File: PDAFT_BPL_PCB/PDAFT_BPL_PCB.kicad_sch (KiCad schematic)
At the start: 16 parts

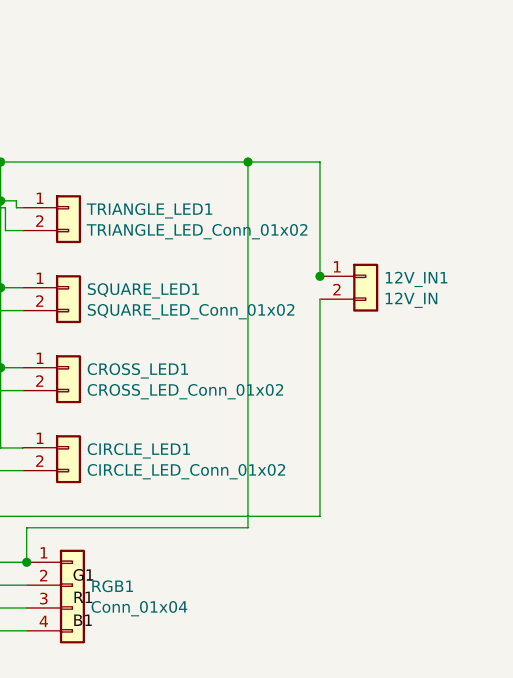
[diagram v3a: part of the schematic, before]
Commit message: Changing 12vin JST XH2 to XH4
Changing 12Vin JST XH2 to XH4 because of possible current rating limits 3A, so better to parallelize 12Vin to avoid problems with it
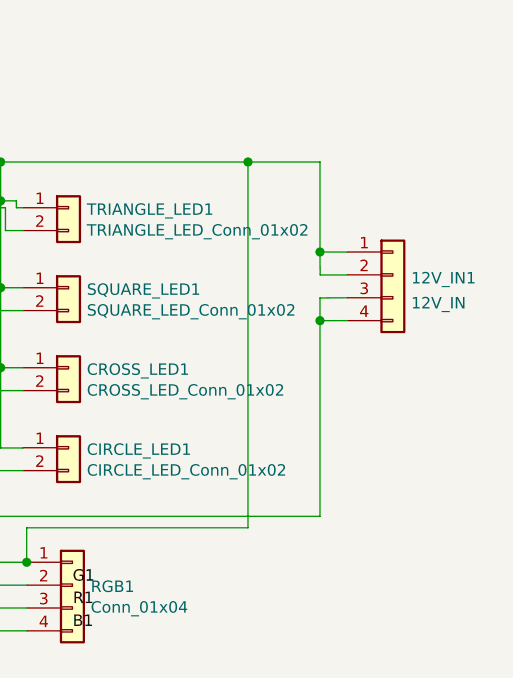
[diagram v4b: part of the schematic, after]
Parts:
- removed 12V_IN1: 12V_IN, Connector_JST:JST_XH_B2B-XH-A_1x02_P2.50mm_Vertical, symbol Connector_Generic:Conn_01x02
- added 12V_IN1: 12V_IN, Connector_JST:JST_XH_B4B-XH-A_1x04_P2.50mm_Vertical, symbol Connector_Generic:Conn_01x04
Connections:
- net at Circle1.3 (Pin_3), Cross1.3 (Pin_3), ProMicro1.23 (GND)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: now also 12V_IN1.3 (Pin_3), 12V_IN1.4 (Pin_4)
- net at CIRCLE_LED1.1 (Pin_1), CROSS_LED1.1 (Pin_1), RGB1.1 (Pin_1)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: now also 12V_IN1.1 (Pin_1), 12V_IN1.2 (Pin_2)
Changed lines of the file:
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@@
   (junction (at 217.6018 85.1154) (diameter 1.016) (color 0 0 0 0))
   (junction (at 242.189 40.64) (diameter 1.016) (color 0 0 0 0))
-  (junction (at 250.19 53.34) (diameter 1.016) (color 0 0 0 0))
+  (junction (at 250.19 50.6406) (diameter 1.016) (color 0 0 0 0))
+  (junction (at 250.19 58.2723) (diameter 1.016) (color 0 0 0 0))
   (wire (pts (xy 43.0276 40.7162) (xy 43.0276 63.3222))
     (stroke (width 0) (type solid) (color 0 0 0 0))
@@
     (stroke (width 0) (type solid) (color 0 0 0 0))
   )
-  (wire (pts (xy 250.19 40.64) (xy 250.19 53.34))
-    (stroke (width 0) (type solid) (color 0 0 0 0))
-  )
-  (wire (pts (xy 250.19 53.34) (xy 250.19 53.3654))
-    (stroke (width 0) (type solid) (color 0 0 0 0))
-  )
-  (wire (pts (xy 250.19 55.88) (xy 250.19 80.01))
+  (wire (pts (xy 250.19 40.64) (xy 250.19 50.6406))
+    (stroke (width 0) (type solid) (color 0 0 0 0))
+  )
+  (wire (pts (xy 250.19 50.6406) (xy 250.19 50.6463))
+    (stroke (width 0) (type solid) (color 0 0 0 0))
+  )
+  (wire (pts (xy 250.19 50.6406) (xy 250.2094 53.1851))
+    (stroke (width 0) (type solid) (color 0 0 0 0))
+  )
+  (wire (pts (xy 250.19 55.7447) (xy 250.19 58.2723))
+    (stroke (width 0) (type solid) (color 0 0 0 0))
+  )
+  (wire (pts (xy 250.19 55.7447) (xy 253.2055 55.7251))
+    (stroke (width 0) (type solid) (color 0 0 0 0))
+  )
+  (wire (pts (xy 250.19 58.2723) (xy 250.19 80.01))
+    (stroke (width 0) (type solid) (color 0 0 0 0))
+  )
+  (wire (pts (xy 250.2094 53.1851) (xy 253.2055 53.1851))
+    (stroke (width 0) (type solid) (color 0 0 0 0))
+  )
+  (wire (pts (xy 253.2055 50.6451) (xy 250.19 50.6463))
+    (stroke (width 0) (type solid) (color 0 0 0 0))
+  )
+  (wire (pts (xy 253.2055 58.2651) (xy 250.19 58.2723))
     (stroke (width 0) (type solid) (color 0 0 0 0))
   )
@@
     )
     (property "Datasheet" "~" (id 3) (at 222.25 72.39 0)
-      (effects (font (size 1.27 1.27)) hide)
-    )
-    (pin "1")
-    (pin "2")
-  )
-  (symbol (lib_id "Connector_Generic:Conn_01x02") (at 255.27 53.34 0) (unit 1)
-    (in_bom yes) (on_board yes)
-    (property "Reference" "12V_IN1" (id 0) (at 257.302 53.5432 0)
-      (effects (font (size 1.27 1.27)) (justify left))
-    )
-    (property "Value" "12V_IN" (id 1) (at 257.302 55.8546 0)
-      (effects (font (size 1.27 1.27)) (justify left))
-    )
-    (property "Footprint" "Connector_JST:JST_XH_B2B-XH-A_1x02_P2.50mm_Vertical" (id 2) (at 255.27 53.34 0)
-      (effects (font (size 1.27 1.27)) hide)
-    )
-    (property "Datasheet" "~" (id 3) (at 255.27 53.34 0)
       (effects (font (size 1.27 1.27)) hide)
     )
@@
     )
     (property "Datasheet" "~" (id 3) (at 222.6818 87.6554 0)
+      (effects (font (size 1.27 1.27)) hide)
+    )
+    (pin "1")
+    (pin "2")
+    (pin "3")
+    (pin "4")
+  )
+  (symbol (lib_id "Connector_Generic:Conn_01x04") (at 258.2855 53.1851 0) (unit 1)
+    (in_bom yes) (on_board yes) (fields_autoplaced)
+    (property "Reference" "12V_IN1" (id 0) (at 260.3176 53.5466 0)
+      (effects (font (size 1.27 1.27)) (justify left))
+    )
+    (property "Value" "12V_IN" (id 1) (at 260.3176 56.3217 0)
+      (effects (font (size 1.27 1.27)) (justify left))
+    )
+    (property "Footprint" "Connector_JST:JST_XH_B4B-XH-A_1x04_P2.50mm_Vertical" (id 2) (at 258.2855 53.1851 0)
+      (effects (font (size 1.27 1.27)) hide)
+    )
+    (property "Datasheet" "~" (id 3) (at 258.2855 53.1851 0)
       (effects (font (size 1.27 1.27)) hide)
     )
@@
   )
   (symbol_instances
-    (path "/00000000-0000-0000-0000-00005dc75aa5"
-      (reference "12V_IN1") (unit 1) (value "12V_IN") (footprint "Connector_JST:JST_XH_B2B-XH-A_1x02_P2.50mm_Vertical")
+    (path "/bfd26073-15dd-489a-abdd-d9c873eed720"
+      (reference "12V_IN1") (unit 1) (value "12V_IN") (footprint "Connector_JST:JST_XH_B4B-XH-A_1x04_P2.50mm_Vertical")
     )
     (path "/00000000-0000-0000-0000-00005dc6eebc"

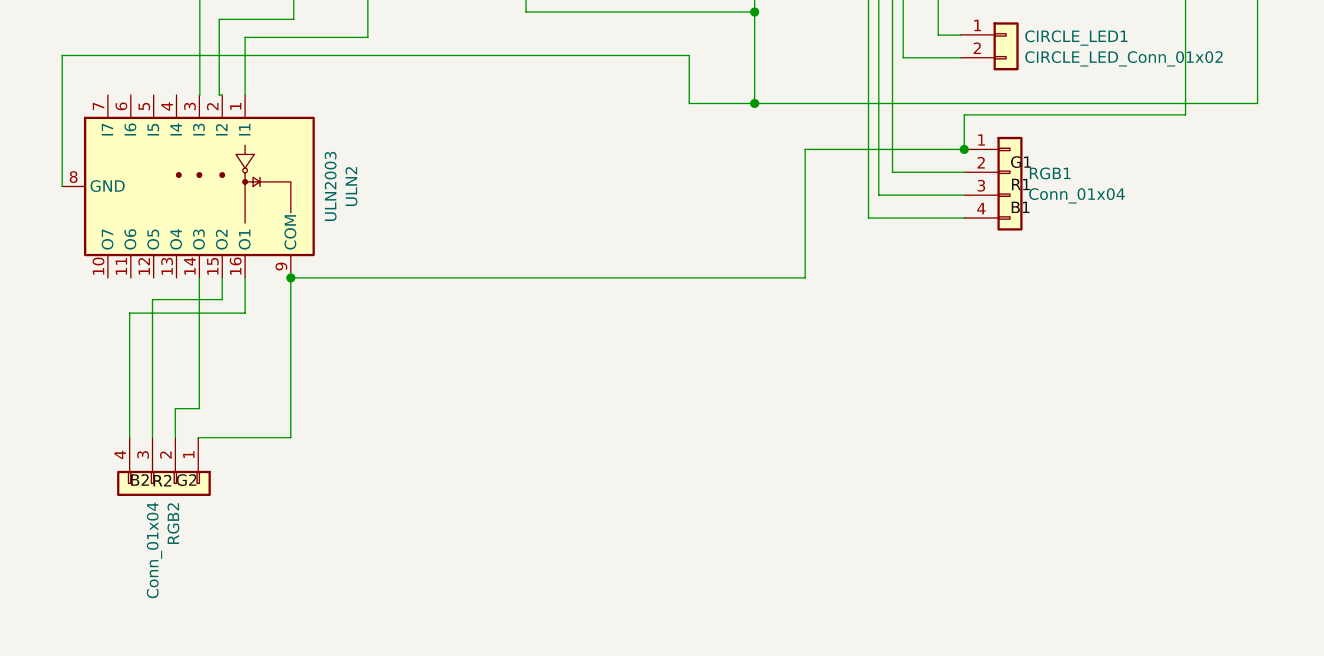
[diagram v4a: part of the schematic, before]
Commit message: Firmware update
Firmware updated (USB-Serial and serial1 different firmware files), added 3D-model of Arduino for picture, pictures added, readme updated
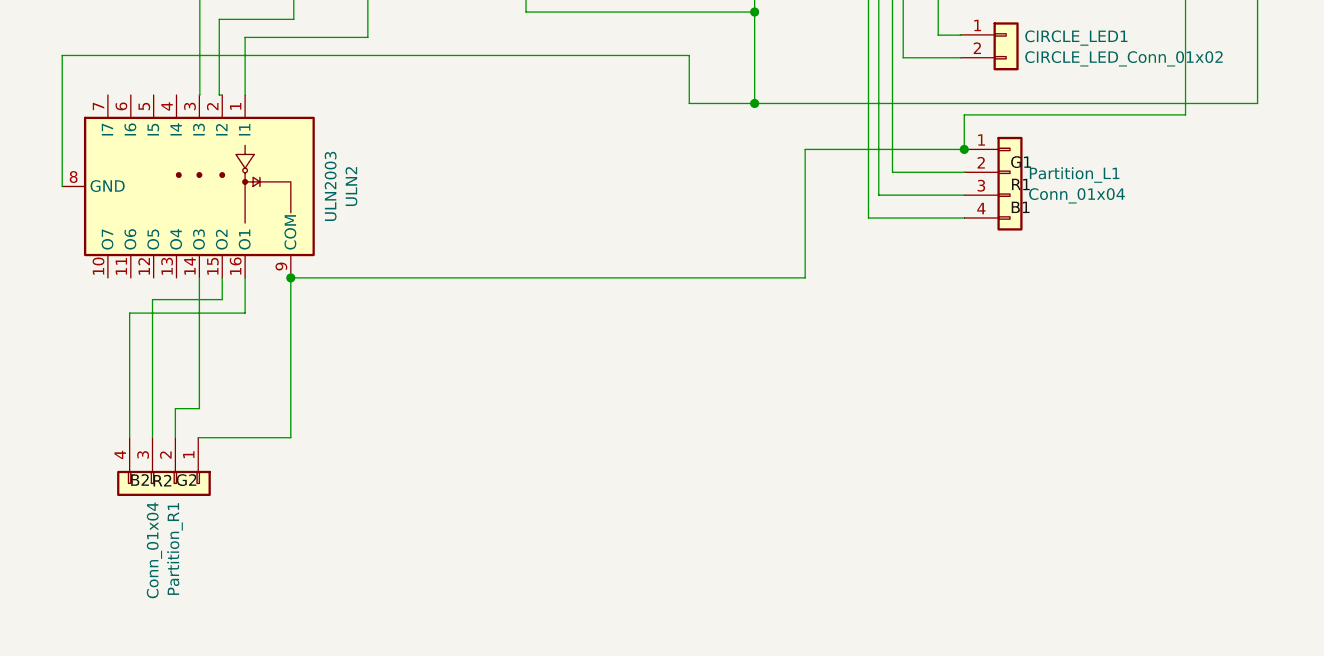
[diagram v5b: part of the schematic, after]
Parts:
- renumbered RGB1 to Partition_L1, RGB2 to Partition_R1
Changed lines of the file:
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@@
   (symbol (lib_id "Connector_Generic:Conn_01x04") (at 129.9464 122.2248 270) (unit 1)
     (in_bom yes) (on_board yes)
-    (property "Reference" "RGB2" (id 0) (at 129.7748 124.2574 0)
+    (property "Reference" "Partition_R1" (id 0) (at 129.7748 124.2574 0)
       (effects (font (size 1.27 1.27)) (justify left))
     )
@@
   (symbol (lib_id "Connector_Generic:Conn_01x04") (at 222.6818 87.6554 0) (unit 1)
     (in_bom yes) (on_board yes)
-    (property "Reference" "RGB1" (id 0) (at 224.7144 87.8268 0)
+    (property "Reference" "Partition_L1" (id 0) (at 224.7144 87.8268 0)
       (effects (font (size 1.27 1.27)) (justify left))
     )
@@
       (reference "Cross1") (unit 1) (value "Cross_Conn_01x03") (footprint "Connector_JST:JST_XH_B3B-XH-A_1x03_P2.50mm_Vertical")
     )
+    (path "/de228416-166c-4c74-8263-2f3b345625f3"
+      (reference "Partition_L1") (unit 1) (value "Conn_01x04") (footprint "Connector_JST:JST_XH_B4B-XH-A_1x04_P2.50mm_Vertical")
+    )
+    (path "/aef4d4d7-e37f-4507-884d-3c54c0de4ff8"
+      (reference "Partition_R1") (unit 1) (value "Conn_01x04") (footprint "Connector_JST:JST_XH_B4B-XH-A_1x04_P2.50mm_Vertical")
+    )
     (path "/00000000-0000-0000-0000-00005dc18eee"
       (reference "ProMicro1") (unit 1) (value "ProMicro") (footprint "promicro:ProMicro")
     )
-    (path "/de228416-166c-4c74-8263-2f3b345625f3"
-      (reference "RGB1") (unit 1) (value "Conn_01x04") (footprint "Connector_JST:JST_XH_B4B-XH-A_1x04_P2.50mm_Vertical")
-    )
-    (path "/aef4d4d7-e37f-4507-884d-3c54c0de4ff8"
-      (reference "RGB2") (unit 1) (value "Conn_01x04") (footprint "Connector_JST:JST_XH_B4B-XH-A_1x04_P2.50mm_Vertical")
-    )
     (path "/00000000-0000-0000-0000-00005dc6de66"
